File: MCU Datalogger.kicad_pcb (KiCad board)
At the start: 2 copper layers, 52.1 x 31.7 mm, 29 parts, among them J1 Conn_01x04_Pin, J2 Conn_01x04_Pin, J3 Conn_01x09_Pin, J4 Conn_02x03_Odd_Even, U1 24LC1025, U2 24LC1025, U3 DS1337S_, U4 ATMEGA328P-AU, Y1 32.768 KHZ, Y2 16 MHz

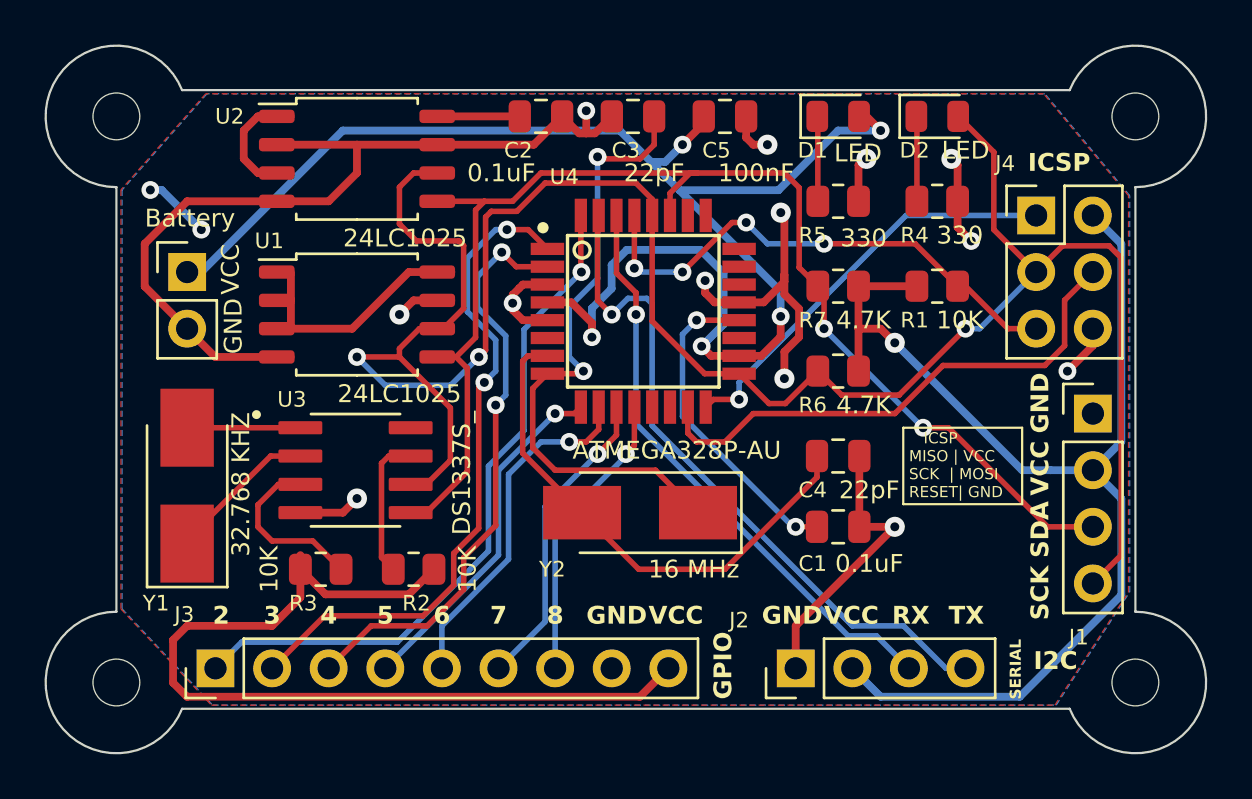
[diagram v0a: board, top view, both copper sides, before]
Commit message: Completed 4-layer pcb routing.
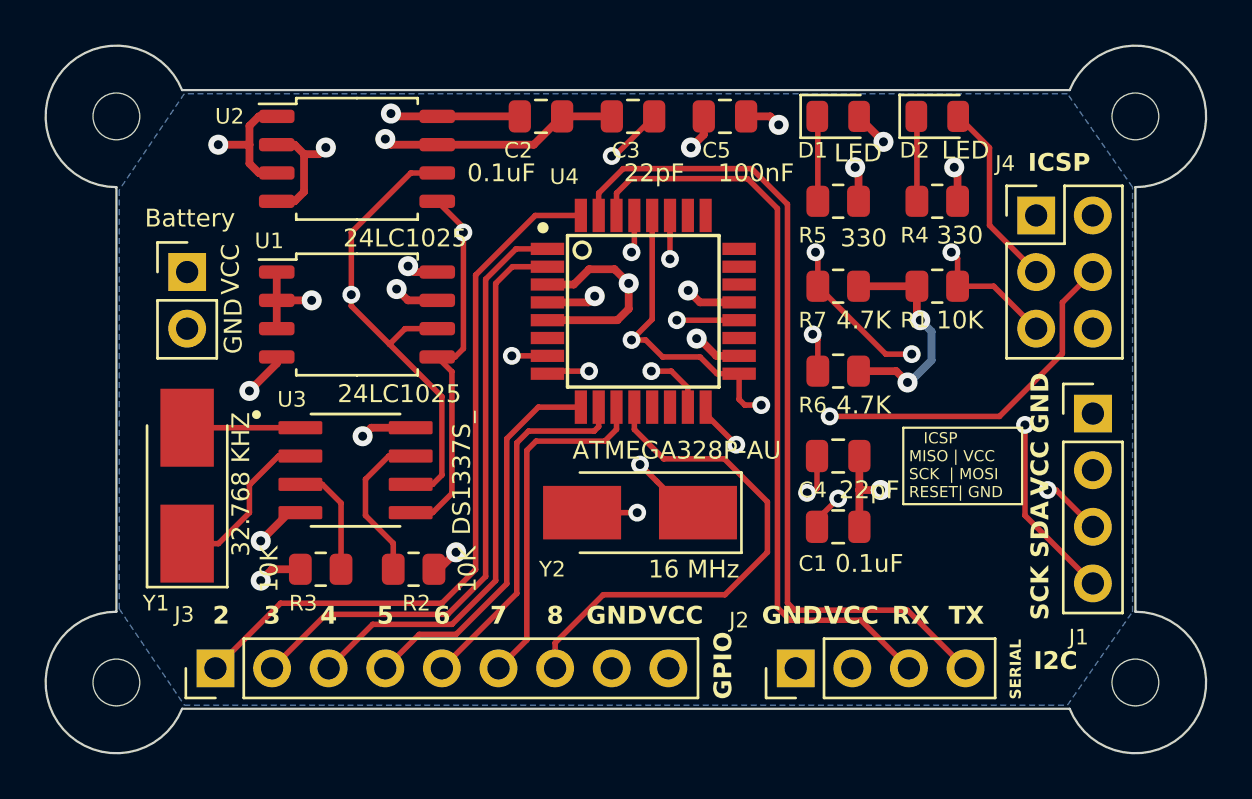
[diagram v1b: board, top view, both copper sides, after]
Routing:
- net /Vcc: track 186.0 -> 46.0 mm, vias 8 -> 13
- net GND: track 83.9 -> 43.4 mm, vias 13 -> 11
- net /SCK: track 100.8 -> 90.5 mm, vias 3 -> 5
- net /D8: track 13.2 -> 22.9 mm, vias 1 -> 0
- net Net-(U4-AREF): track 14.6 -> 23.4 mm
- net /RX: track 26.5 -> 34.0 mm, vias 1 -> 0
- net /TX: track 31.0 -> 37.7 mm, vias 1 -> 0
- net /MISO: track 18.8 -> 23.1 mm
- net /MOSI: track 23.8 -> 27.8 mm, vias 0 -> 2
- net Net-(U4-PB7): track 28.4 -> 24.5 mm, vias 2 -> 3
- net /SDA: track 57.0 -> 54.0 mm, vias 2 -> 5
- net Net-(U3-~{INTA}): track 7.79 -> 5.14 mm
- net /D3: track 30.2 -> 28.0 mm, vias 2 -> 0
- net /D7: track 13.9 -> 15.7 mm, vias 1 -> 0
- net /D4: track 26.7 -> 25.1 mm, vias 2 -> 0
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- added copper zone on In2.Cu, net /Vcc
- removed copper zone on F.Cu, net /Vcc
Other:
- copper layers 2 -> 4

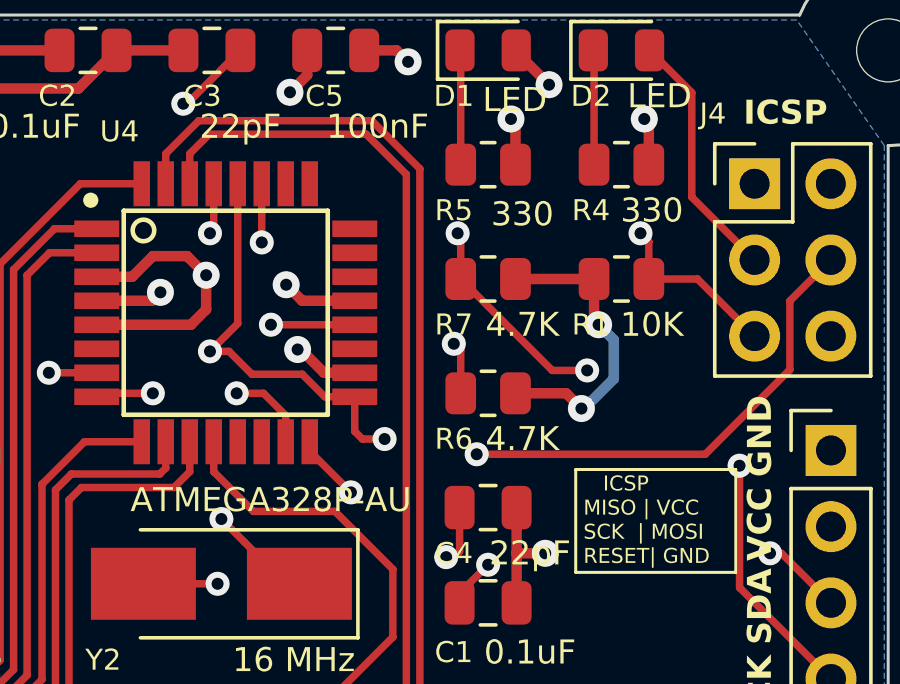
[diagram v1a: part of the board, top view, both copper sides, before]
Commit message: Fixed net bugs in 4 layer version of the PCB.
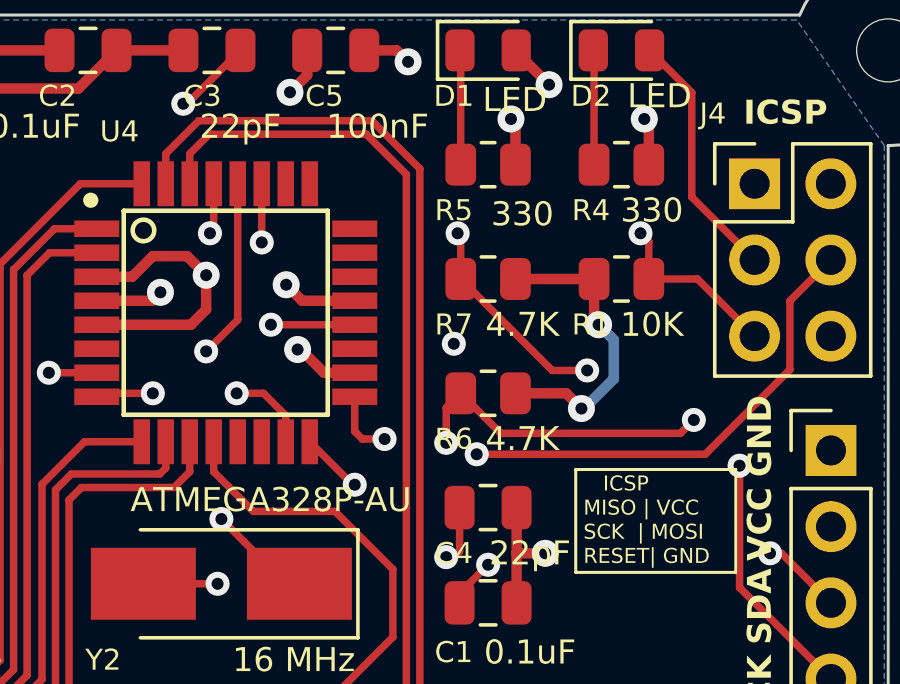
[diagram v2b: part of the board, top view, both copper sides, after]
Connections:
- J1 pad 4: /SCK -> /SCL
- R6 pad 2: /SCK -> /SCL
- U1 pad 6: /SCK -> /SCL
- U2 pad 6: /SCK -> /SCL
- U3 pad 6: /SCK -> /SCL
- U4 pad 28: /SCK -> /SCL
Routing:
- net /SCL: track 0.00 -> 73.7 mm, vias 0 -> 5
- net /SCK: track 90.5 -> 26.4 mm, vias 5 -> 2
- net /MISO: track 23.1 -> 22.3 mm
